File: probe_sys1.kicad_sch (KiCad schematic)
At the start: 23 parts, among them J1 Screw_Terminal_01x02

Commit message: RPI, RN, ESP.
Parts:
- removed D1, D2: LED, LED_SMD:LED_0603_1608Metric_Pad1.05x0.95mm_HandSolder, symbol Device:LED
- removed J1: Screw_Terminal_01x02, PEP_library:TerminalBlock_Phoenix_MKDS-1,5-2-5.08_1x02_P5.08mm_Horizontal, symbol Connector:Screw_Terminal_01x02
- removed JP1, JP2, JP3, JP4, JP5, JP6, JP7, JP8: Jumper, Connector_PinHeader_2.54mm:PinHeader_1x02_P2.54mm_Vertical, symbol Jumper:Jumper_2_Bridged
- removed R1, R6: 300, PEP_library:R_smd, symbol Device:R
- removed R2, R3, R5, R8: 4.7k, PEP_library:R_smd, symbol Device:R
- removed R4, R7: 1k, PEP_library:R_smd, symbol Device:R
- added MODULE1: RN2483-I_RM095, probe_sys1:RN2483-I_RM095, symbol probe_sys1:RN2483-I_RM095
- added U1: ESP32-WROOM-32UE, RF_Module:ESP32-WROOM-32UE, symbol RF_Module:ESP32-WROOM-32UE
- added U2: RASPBERRY_PI_ZERO_2_W, probe_sys1:MODULE_RASPBERRY_PI_ZERO_2_W, symbol probe_sys1:RASPBERRY_PI_ZERO_2_W
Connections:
- new net: MODULE1.1 (GND), MODULE1.11 (GND), MODULE1.20 (GND), MODULE1.21 (GND), MODULE1.22 (GND), MODULE1.24 (GND), MODULE1.26 (GND), MODULE1.27 (GND), MODULE1.28 (GND), MODULE1.33 (GND), MODULE1.41 (GND), MODULE1.47 (GND), MODULE1.8 (GND)
- new net: U1.1 (GND), U1.15 (GND), U1.38 (GND), U1.39 (GND)

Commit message: SIM, wroom.
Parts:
- added U3: SIM808, probe_sys1:SIM808, symbol probe_sys1:SIM808
- U1: footprint RF_Module:ESP32-WROOM-32UE -> probe_sys1:ESP32-WROOM-32UE
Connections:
- new net: U3.1 (GND), U3.18 (GND), U3.2 (GND), U3.28 (GND), U3.3 (GND), U3.34 (GND), U3.36 (GND), U3.40 (GND), U3.51 (GND), U3.52 (GND), U3.54 (GND), U3.64 (GND), U3.65 (GND), U3.67 (GND), U3.68 (GND)
- new net: U3.4 (VBAT), U3.5 (VBAT), U3.6 (VBAT)

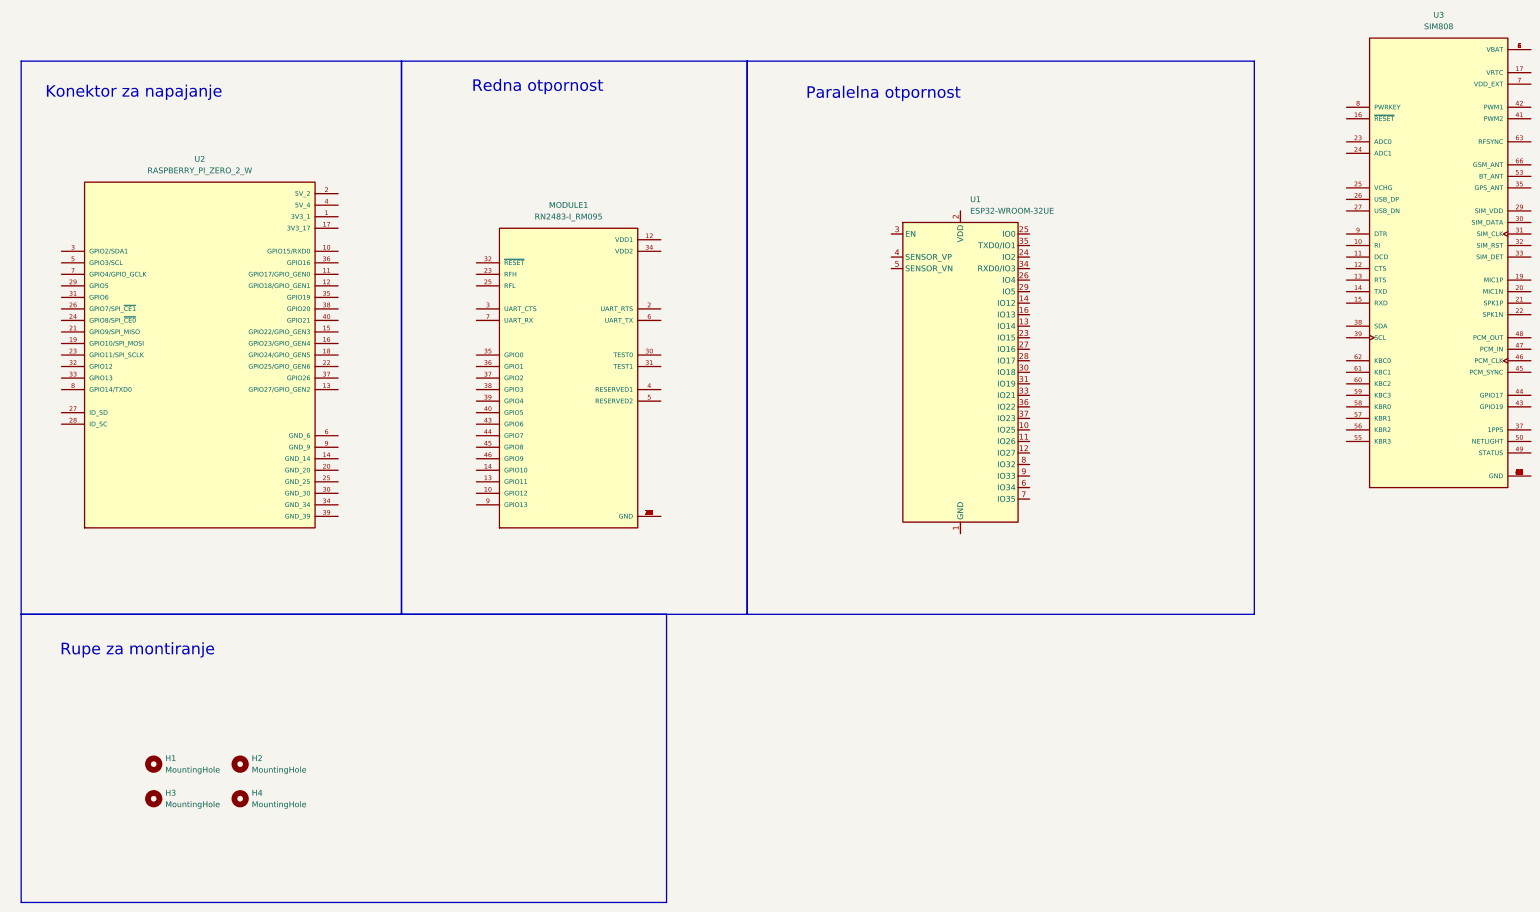
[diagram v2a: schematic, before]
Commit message: Started connecting IC pins
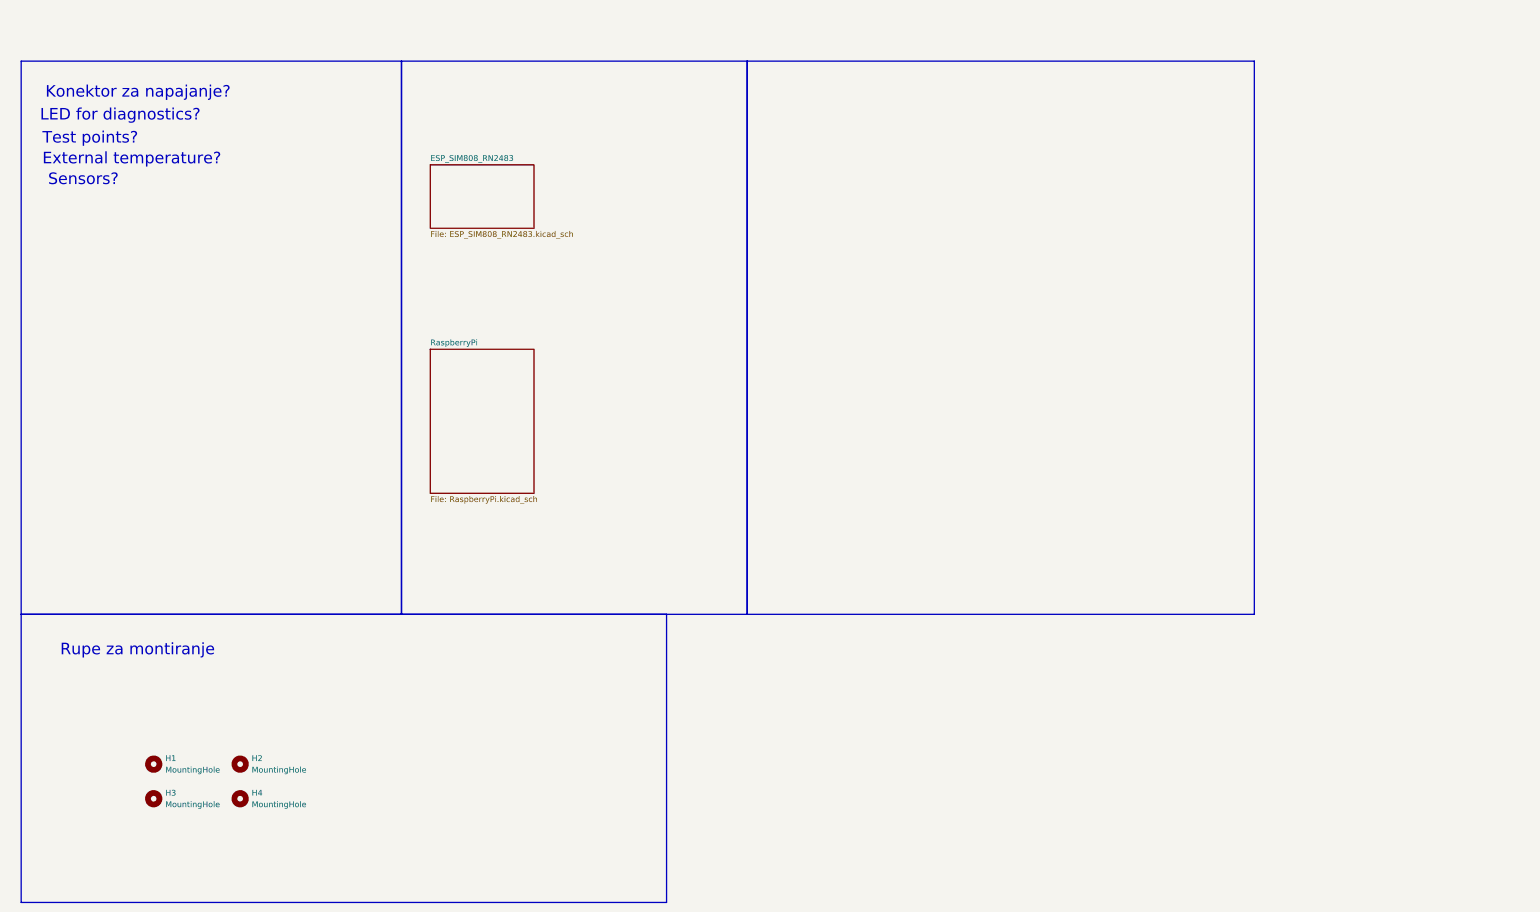
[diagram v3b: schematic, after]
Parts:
- removed MODULE1: RN2483-I_RM095, probe_sys1:RN2483-I_RM095, symbol probe_sys1:RN2483-I_RM095
- removed U1: ESP32-WROOM-32UE, probe_sys1:ESP32-WROOM-32UE, symbol RF_Module:ESP32-WROOM-32UE
- removed U2: RASPBERRY_PI_ZERO_2_W, probe_sys1:MODULE_RASPBERRY_PI_ZERO_2_W, symbol probe_sys1:RASPBERRY_PI_ZERO_2_W
- removed U3: SIM808, probe_sys1:SIM808, symbol probe_sys1:SIM808
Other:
- added sheet ESP_SIM808_RN2483 (ESP_SIM808_RN2483.kicad_sch)
- added sheet RaspberryPi (RaspberryPi.kicad_sch)
- note added: "External temperature?"
- note added: "Konektor za napajanje?"
- note added: "LED for diagnostics?"
- note added: "Sensors?"
- note added: "Test points?"
- note removed: "Konektor za napajanje"
- note removed: "Paralelna otpornost"
- note removed: "Redna otpornost"
- title: Redna i paralelna otpornost -> ##Redna i paralelna otpornost
